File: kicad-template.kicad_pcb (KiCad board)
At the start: 2 copper layers, 30 x 25 mm, 4 parts

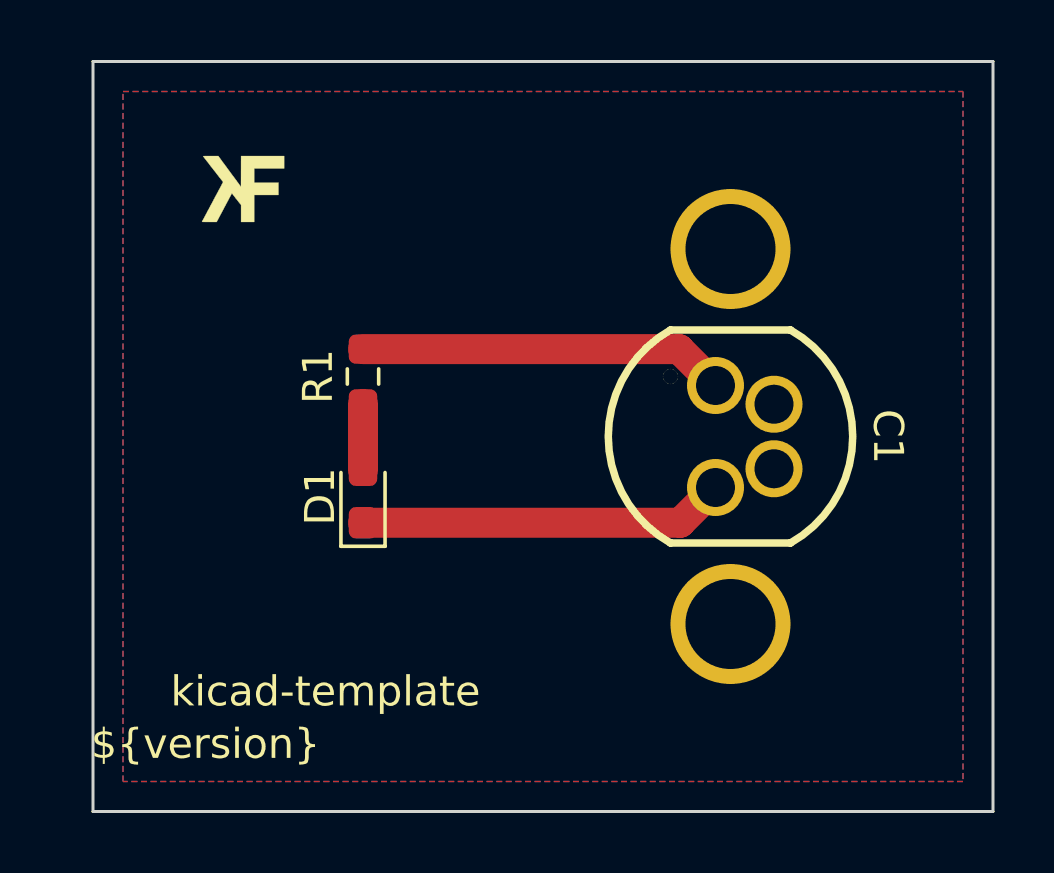
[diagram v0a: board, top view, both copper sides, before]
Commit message: feat: switched to 4-Layer PCB; updated DRU SMD Pad to Pad clearance
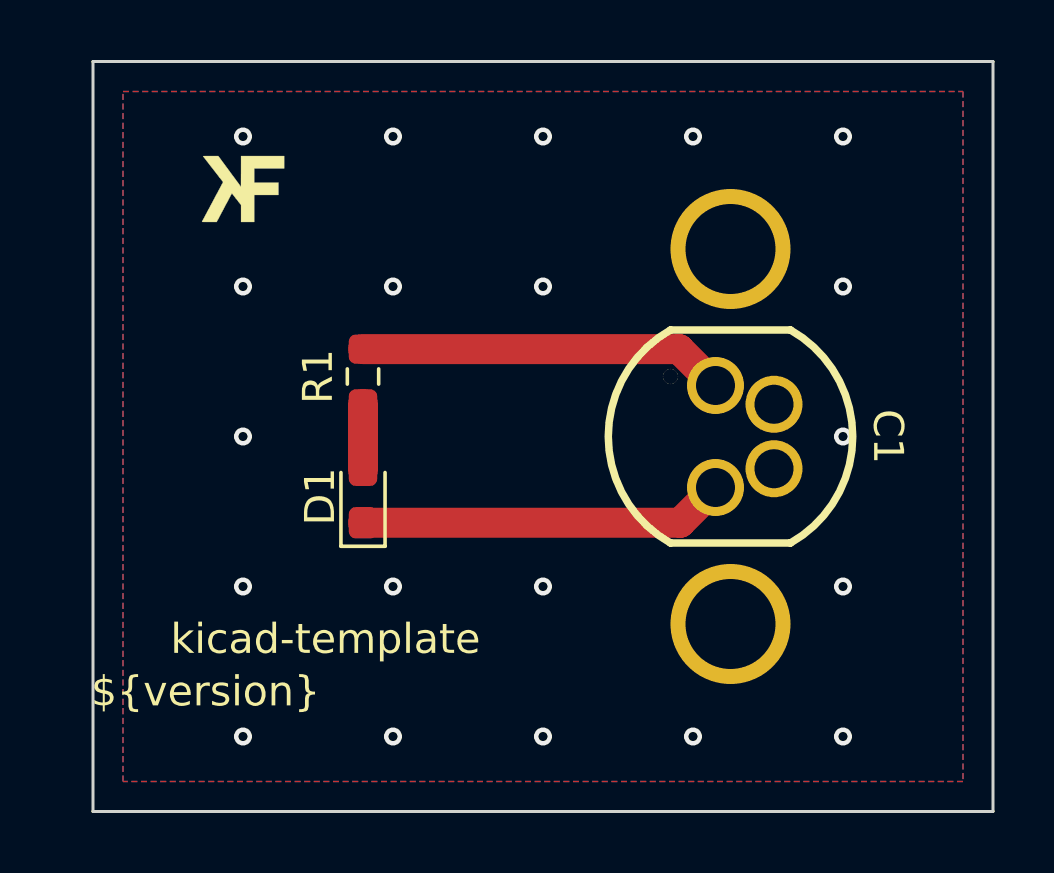
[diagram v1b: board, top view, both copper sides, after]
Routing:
- net GND: vias 0 -> 20
- added copper zone on In1.Cu, net GND
- added copper zone on In2.Cu, net GND
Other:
- copper layers 2 -> 4
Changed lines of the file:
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@@
 	(layers
 		(0 "F.Cu" signal)
+		(1 "In1.Cu" signal)
+		(2 "In2.Cu" signal)
 		(31 "B.Cu" signal)
 		(32 "B.Adhes" user "B.Adhesive")
@@
 			)
 			(layer "dielectric 1"
-				(type "core")
-				(thickness 1.51)
+				(type "prepreg")
+				(thickness 0.1)
 				(material "FR4")
 				(epsilon_r 4.5)
 				(loss_tangent 0.02)
 			)
+			(layer "In1.Cu"
+				(type "copper")
+				(thickness 0.035)
+			)
+			(layer "dielectric 2"
+				(type "core")
+				(thickness 1.24)
+				(material "FR4")
+				(epsilon_r 4.5)
+				(loss_tangent 0.02)
+			)
+			(layer "In2.Cu"
+				(type "copper")
+				(thickness 0.035)
+			)
+			(layer "dielectric 3"
+				(type "prepreg")
+				(thickness 0.1)
+				(material "FR4")
+				(epsilon_r 4.5)
+				(loss_tangent 0.02)
+			)
 			(layer "B.Cu"
 				(type "copper")
@@
 		)
 		(pad_to_mask_clearance 0)
+		(solder_mask_min_width 0.1)
 		(allow_soldermask_bridges_in_footprints no)
 		(pcbplotparams
@@
 	)
 	(gr_text "${version}"
-		(at 63.75 55.25 0)
+		(at 63.75 53.5 0)
 		(layer "F.SilkS")
 		(effects
@@
 	)
 	(gr_text "kicad-template"
-		(at 67.75 53.5 0)
+		(at 67.75 51.75 0)
 		(layer "F.SilkS")
 		(effects
@@
 		(net 3)
 	)
+	(via
+		(at 65 40)
+		(size 0.6)
+		(drill 0.3)
+		(layers "F.Cu" "B.Cu")
+		(free yes)
+		(net 3)
+	)
+	(via
+		(at 75 40)
+		(size 0.6)
+		(drill 0.3)
+		(layers "F.Cu" "B.Cu")
+		(free yes)
+		(net 3)
+	)
+	(via
+		(at 65 45)
+		(size 0.6)
+		(drill 0.3)
+		(layers "F.Cu" "B.Cu")
+		(free yes)
+		(net 3)
+	)
+	(via
+		(at 65 35)
+		(size 0.6)
+		(drill 0.3)
+		(layers "F.Cu" "B.Cu")
+		(free yes)
+		(net 3)
+	)
+	(via
+		(at 85 45)
+		(size 0.6)
+		(drill 0.3)
+		(layers "F.Cu" "B.Cu")
+		(free yes)
+		(net 3)
+	)
+	(via
+		(at 85 50)
+		(size 0.6)
+		(drill 0.3)
+		(layers "F.Cu" "B.Cu")
+		(free yes)
+		(net 3)
+	)
+	(via
+		(at 80 35)
+		(size 0.6)
+		(drill 0.3)
+		(layers "F.Cu" "B.Cu")
+		(free yes)
+		(net 3)
+	)
+	(via
+		(at 85 35)
+		(size 0.6)
+		(drill 0.3)
+		(layers "F.Cu" "B.Cu")
+		(free yes)
+		(net 3)
+	)
+	(via
+		(at 70 35)
+		(size 0.6)
+		(drill 0.3)
+		(layers "F.Cu" "B.Cu")
+		(free yes)
+		(net 3)
+	)
+	(via
+		(at 65 55)
+		(size 0.6)
+		(drill 0.3)
+		(layers "F.Cu" "B.Cu")
+		(free yes)
+		(net 3)
+	)
+	(via
+		(at 65 50)
+		(size 0.6)
+		(drill 0.3)
+		(layers "F.Cu" "B.Cu")
+		(free yes)
+		(net 3)
+	)
+	(via
+		(at 75 50)
+		(size 0.6)
+		(drill 0.3)
+		(layers "F.Cu" "B.Cu")
+		(free yes)
+		(net 3)
+	)
+	(via
+		(at 85 40)
+		(size 0.6)
+		(drill 0.3)
+		(layers "F.Cu" "B.Cu")
+		(free yes)
+		(net 3)
+	)
+	(via
+		(at 70 55)
+		(size 0.6)
+		(drill 0.3)
+		(layers "F.Cu" "B.Cu")
+		(free yes)
+		(net 3)
+	)
+	(via
+		(at 80 55)
+		(size 0.6)
+		(drill 0.3)
+		(layers "F.Cu" "B.Cu")
+		(free yes)
+		(net 3)
+	)
+	(via
+		(at 75 55)
+		(size 0.6)
+		(drill 0.3)
+		(layers "F.Cu" "B.Cu")
+		(free yes)
+		(net 3)
+	)
+	(via
+		(at 70 40)
+		(size 0.6)
+		(drill 0.3)
+		(layers "F.Cu" "B.Cu")
+		(free yes)
+		(net 3)
+	)
+	(via
+		(at 70 50)
+		(size 0.6)
+		(drill 0.3)
+		(layers "F.Cu" "B.Cu")
+		(free yes)
+		(net 3)
+	)
+	(via
+		(at 85 55)
+		(size 0.6)
+		(drill 0.3)
+		(layers "F.Cu" "B.Cu")
+		(free yes)
+		(net 3)
+	)
+	(via
+		(at 75 35)
+		(size 0.6)
+		(drill 0.3)
+		(layers "F.Cu" "B.Cu")
+		(free yes)
+		(net 3)
+	)
 	(segment
 		(start 69 43.9125)
@@
 		(net 3)
 		(net_name "GND")
-		(layers "F&B.Cu")
+		(layers "F.Cu" "In1.Cu" "In2.Cu" "B.Cu")
 		(hatch edge 0.508)
 		(connect_pads
